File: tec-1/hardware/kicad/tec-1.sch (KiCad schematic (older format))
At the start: 34 parts

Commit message: tec-1/hardware/kicad: progress checkin
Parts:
- removed C? (x4): 0.1uF/10V, symbol tec-1:C
- removed C?: 100uF/10V, symbol tec-1:C
- removed FB?: Ferrite_Bead_Small, symbol tec-1:Ferrite_Bead_Small
- removed J?: USB_C_Receptacle_USB2.0, symbol tec-1:USB_C_Receptacle_USB2.0
- removed R?: 100k, symbol tec-1:R
- removed R? (x2): 5.1k, symbol tec-1:R
- removed U?: ADDRESS, symbol tec-1:ADDRESS
- removed U?: KEYDB, symbol tec-1:KEYDB
- removed U?: FT232RL, Package_SO:SSOP-28_5.3x10.2mm_P0.65mm, symbol tec-1:FT232RL
- added C1: 0.1uF/10V, tec-1:C_0805_2012Metric, symbol tec-1:C
- added TP1, TP10, TP11, TP12, TP13, TP14, TP15, TP16, TP17, TP18, TP19, TP2, TP20, TP3, TP4, TP5, TP6, TP7, TP8, TP9: TestPoint, tec-1:TestPoint_Pad_D2.0mm, symbol tec-1:TestPoint
- added U1: IO, tec-1:PLCC-28_SMD-Socket, symbol tec-1:IO
- added U2: MEMORY, tec-1:PLCC-28_SMD-Socket, symbol tec-1:MEMORY
- C2, C3, C4, C5, C6: renamed from C?; footprint (none) -> tec-1:C_0805_2012Metric
- R1, R10, R11, R2, R3, R4, R5, R6, R7, R8, R9: renamed from R?; footprint (none) -> tec-1:R_0805_2012Metric
- SW1: renamed from SW?; footprint (none) -> tec-1:DIP-8_W7.62mm_LongPads
- U3: renamed from U?; footprint (none) -> tec-1:DIP-40_W15.24mm_LongPads
- U5, U6: renamed from U?; footprint Package_DIP:DIP-28_W15.24mm -> tec-1:DIP-28_W15.24mm_LongPads
- gave numbers to parts that had none: 1
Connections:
- net labels added: LCD_E, ~MATRIXCOL_G_CS, ~MATRIXCOL_R_CS, ~MATRIXROW_CS, ~SEG7COL_CS, ~SEG7ROW_CS
- net labels removed: FTDI_D0, FTDI_D1, FTDI_D2, FTDI_D3, FTDI_D5, FTDI_D6, FTDI_D7, VBUS
- wire segments 103 -> 123
- no-connect marks 19 -> 14
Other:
- moved on the sheet: C2, R5, R6, R7, R8, SW1

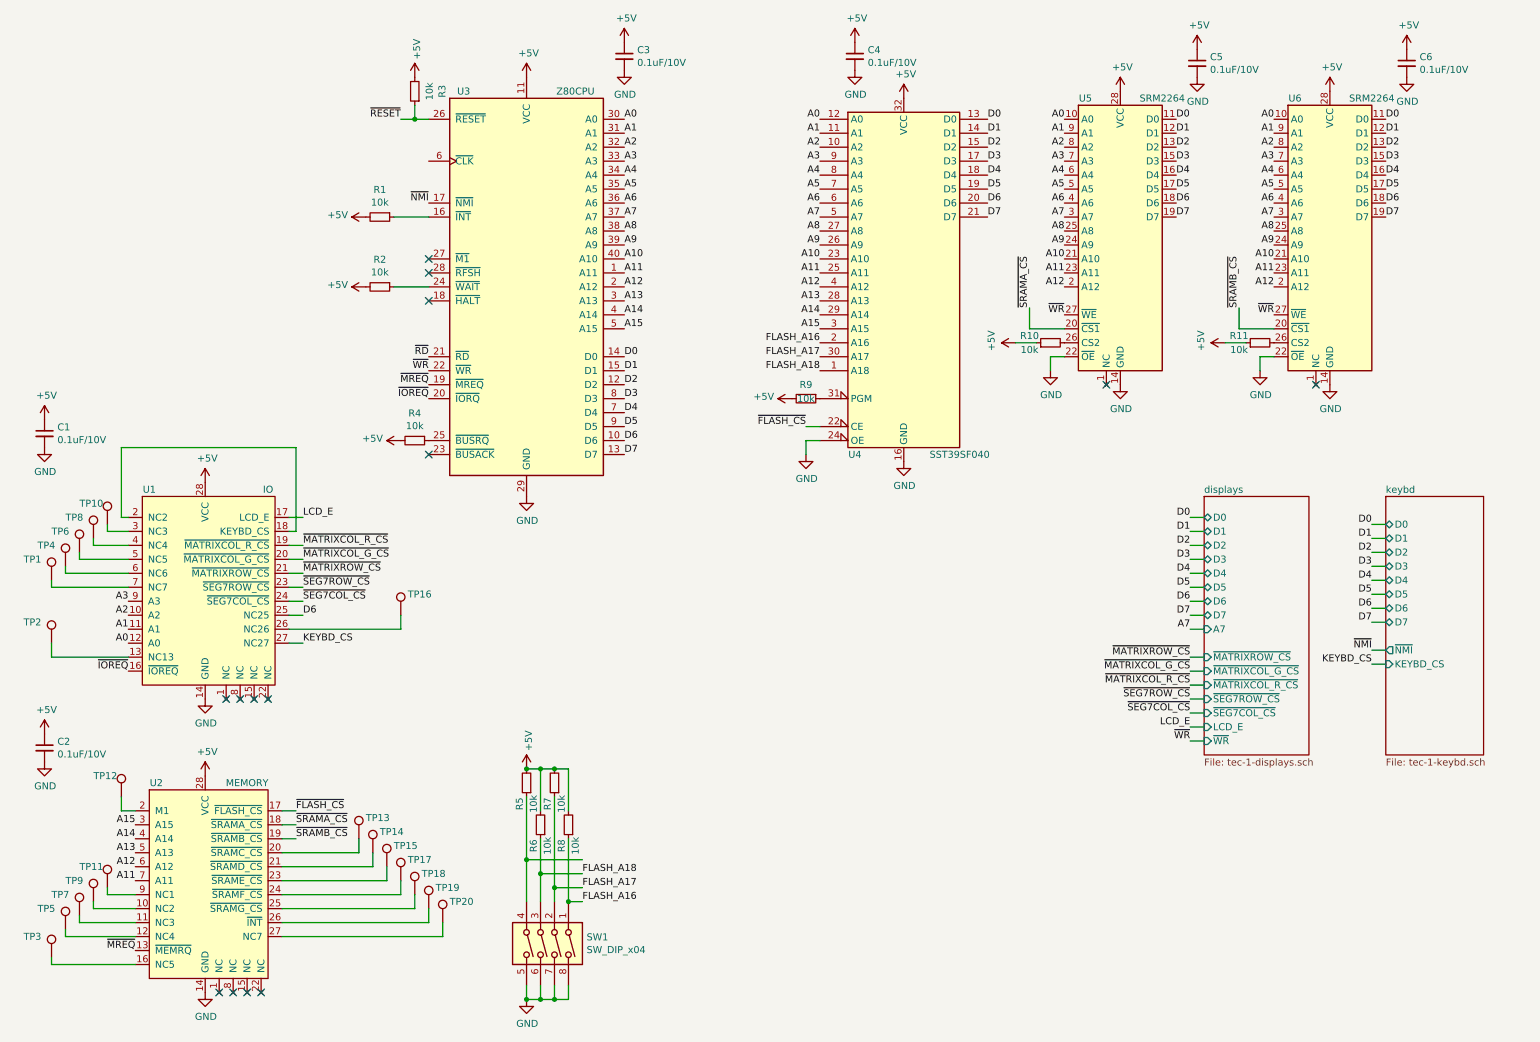
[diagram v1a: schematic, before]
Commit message: tec-1/hardware/kicad: progress checkin - add clock & 207 unrouted
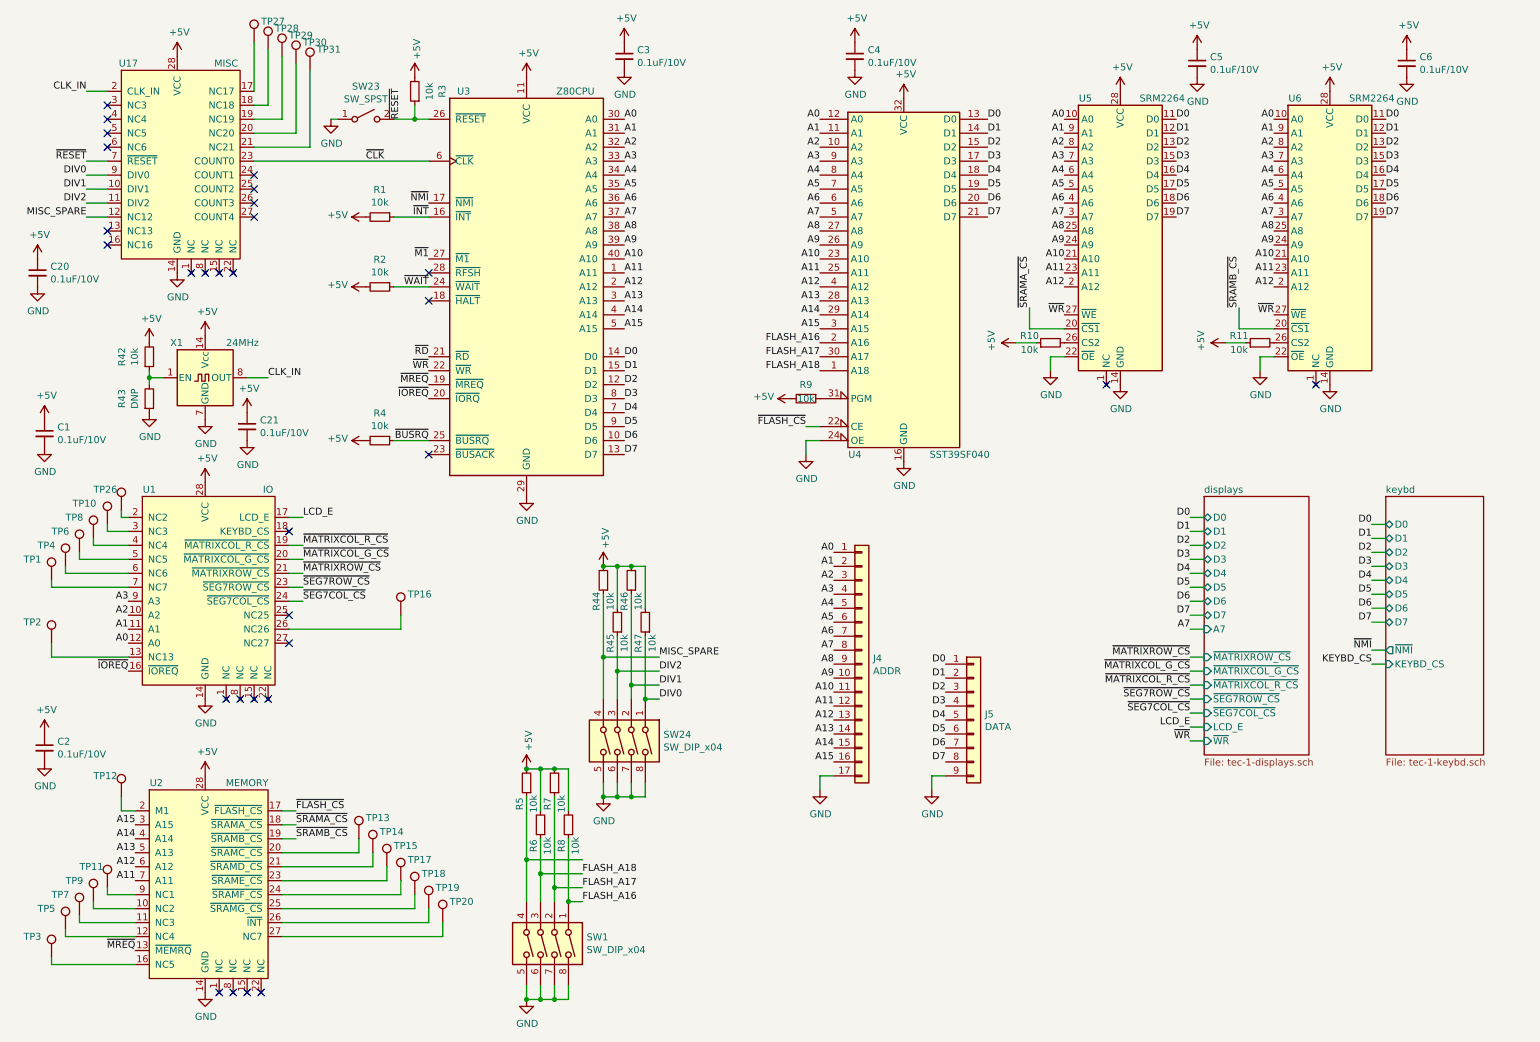
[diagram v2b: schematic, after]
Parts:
- added C20, C21: 0.1uF/10V, tec-1:C_0805_2012Metric, symbol tec-1:C
- added J4: ADDR, tec-1:PinHeader_1x17_P2.54mm_Vertical, symbol tec-1:Conn_01x17
- added J5: DATA, tec-1:PinHeader_1x09_P2.54mm_Vertical, symbol tec-1:Conn_01x09
- added R42, R44, R45, R46, R47: 10k, tec-1:R_0805_2012Metric, symbol tec-1:R
- added R43: DNP, tec-1:R_0805_2012Metric, symbol tec-1:R
- added SW23: SW_SPST, tec-1:SW_12x12_SMD, symbol tec-1:SW_SPST
- added SW24: SW_DIP_x04, tec-1:DIP-8_W7.62mm_LongPads, symbol tec-1:SW_DIP_x04
- added TP26, TP27, TP28, TP29, TP30, TP31: TestPoint, tec-1:TestPoint_Pad_D2.0mm, symbol tec-1:TestPoint
- added U17: MISC, tec-1:PLCC-28_SMD-Socket, symbol tec-1:MISC
- added X1: 24MHz, tec-1:Oscillator_DIP-14_LargePads, symbol tec-1:CXO_DIP14
- U4: footprint (none) -> tec-1:PLCC-32_SMD-Socket_9x7
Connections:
- net +5V: now also C20.1, C21.1, R42.2, R44.2, R45.2, R46.2, R47.2, U17.28 (VCC), X1.14 (Vcc)
- net A0: now also J4.1 (Pin_1)
- net A1: now also J4.2 (Pin_2)
- net A10: now also J4.11 (Pin_11)
- net A11: now also J4.12 (Pin_12)
- net A12: now also J4.13 (Pin_13)
- net A13: now also J4.14 (Pin_14)
- net A14: now also J4.15 (Pin_15)
- net A15: now also J4.16 (Pin_16)
- net A2: now also J4.3 (Pin_3)
- net A3: now also J4.4 (Pin_4)
- net A4: now also J4.5 (Pin_5)
- net A5: now also J4.6 (Pin_6)
- net A6: now also J4.7 (Pin_7)
- net A7: now also J4.8 (Pin_8)
- net A8: now also J4.9 (Pin_9)
- net A9: now also J4.10 (Pin_10)
- net D0: now also J5.1 (Pin_1)
- net D1: now also J5.2 (Pin_2)
- net D2: now also J5.3 (Pin_3)
- net D3: now also J5.4 (Pin_4)
- net D4: now also J5.5 (Pin_5)
- net D5: now also J5.6 (Pin_6)
- net D6: now also J5.7 (Pin_7); no longer U1.25 (NC25)
- net D7: now also J5.8 (Pin_8)
- net GND: now also C20.2, C21.2, J4.17 (Pin_17), J5.9 (Pin_9), R43.1, SW23.1 (A), SW24.5, SW24.6, SW24.7, SW24.8, U17.14 (GND), X1.7 (GND)
- net KEYBD_CS: no longer U1.27 (NC27)
- net ~RESET: now also SW23.2 (B), U17.7 (~RESET)
- net ~INT: now reaches R1.1, U3.16 (~INT~)
- net ~WAIT: now reaches R2.1, U3.24 (~WAIT~)
- net ~BUSRQ: now reaches R4.1, U3.25 (~BUSRQ~)
- net ~M1: now reaches U3.27 (~M1~)
- net ~CLK: now reaches U3.6 (~CLK~)
- net ~CLK: now also U17.23 (COUNT0)
- net at U1.18 (KEYBD_CS): no longer U1.2 (NC2)
- new net: TP27.1, U17.17 (NC17)
- new net: TP28.1, U17.18 (NC18)
- new net: TP29.1, U17.19 (NC19)
- new net: TP30.1, U17.20 (NC20)
- new net: TP31.1, U17.21 (NC21)
- new net: R42.1, R43.2, X1.1 (EN)
- new net: TP26.1, U1.2 (NC2)
- new net CLK_IN: U17.2 (CLK_IN), X1.8 (OUT)
- new net DIV0: R47.1, SW24.1, U17.9 (DIV0)
- new net DIV1: R46.1, SW24.2, U17.10 (DIV1)
- new net DIV2: R45.1, SW24.3, U17.11 (DIV2)
- new net MISC_SPARE: R44.1, SW24.4, U17.12 (NC12)
- no-connect marks 14 -> 30
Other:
- moved on the sheet: R4

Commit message: tec-1/hardware/kicad: routing complete, all DRC errors checked as ok
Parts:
- removed TP10, TP11, TP12, TP14, TP15, TP17, TP19, TP20, TP26, TP4, TP6, TP7, TP8, TP9: TestPoint, tec-1:TestPoint_Pad_D2.0mm, symbol tec-1:TestPoint
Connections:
- net KEYBD_CS: now also U1.18 (KEYBD_CS)
- net ~INT: now also U2.26 (~INT)
- net ~M1: now also U2.2 (M1)
- no-connect marks 30 -> 42
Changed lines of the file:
@@
 Text Label 4800 3650 0    50   ~ 0
 D7
-Text Label 3400 2950 2    50   ~ 0
-~RD
 Text Label 3400 3050 2    50   ~ 0
 ~WR
@@
 	1    0    0    -1
 $EndComp
-$Comp
-L tec-1:TestPoint TP7
-U 1 1 60BE6F95
-P 900 6950
-F 0 "TP7" H 700 7100 50  0000 L CNN
-F 1 "TestPoint" H 958 6977 50  0001 L CNN
-F 2 "tec-1:TestPoint_Pad_D2.0mm" H 1100 6950 50  0001 C CNN
-F 3 "~" H 1100 6950 50  0001 C CNN
-	1    900  6950
-	1    0    0    -1
-$EndComp
-$Comp
-L tec-1:TestPoint TP9
-U 1 1 60BEA0AC
-P 1000 6850
-F 0 "TP9" H 800 7000 50  0000 L CNN
-F 1 "TestPoint" H 1058 6877 50  0001 L CNN
-F 2 "tec-1:TestPoint_Pad_D2.0mm" H 1200 6850 50  0001 C CNN
-F 3 "~" H 1200 6850 50  0001 C CNN
-	1    1000 6850
-	1    0    0    -1
-$EndComp
-$Comp
-L tec-1:TestPoint TP11
-U 1 1 60BEA26C
-P 1100 6750
-F 0 "TP11" H 900 6900 50  0000 L CNN
-F 1 "TestPoint" H 1158 6777 50  0001 L CNN
-F 2 "tec-1:TestPoint_Pad_D2.0mm" H 1300 6750 50  0001 C CNN
-F 3 "~" H 1300 6750 50  0001 C CNN
-	1    1100 6750
-	1    0    0    -1
-$EndComp
-Wire Wire Line
-	1300 6800 1100 6800
-Wire Wire Line
-	1100 6800 1100 6750
-Wire Wire Line
-	1000 6850 1000 6900
-Wire Wire Line
-	1000 6900 1300 6900
-Wire Wire Line
-	1300 7000 900  7000
-Wire Wire Line
-	900  7000 900  6950
 Wire Wire Line
 	1300 7100 800  7100
@@
 	700  7300 1300 7300
 $Comp
-L tec-1:TestPoint TP12
-U 1 1 60BF99B1
-P 1200 6100
-F 0 "TP12" H 1000 6250 50  0000 L CNN
-F 1 "TestPoint" H 1258 6127 50  0001 L CNN
-F 2 "tec-1:TestPoint_Pad_D2.0mm" H 1400 6100 50  0001 C CNN
-F 3 "~" H 1400 6100 50  0001 C CNN
-	1    1200 6100
-	1    0    0    -1
-$EndComp
-Wire Wire Line
-	1200 6100 1200 6200
-Wire Wire Line
-	1200 6200 1300 6200
-$Comp
 L tec-1:TestPoint TP13
 U 1 1 60C03715
@@
 $EndComp
 $Comp
-L tec-1:TestPoint TP14
-U 1 1 60C068C6
-P 3000 6500
-F 0 "TP14" H 3050 6650 50  0000 L CNN
-F 1 "TestPoint" H 3058 6527 50  0001 L CNN
-F 2 "tec-1:TestPoint_Pad_D2.0mm" H 3200 6500 50  0001 C CNN
-F 3 "~" H 3200 6500 50  0001 C CNN
-	1    3000 6500
-	1    0    0    -1
-$EndComp
-$Comp
-L tec-1:TestPoint TP15
-U 1 1 60C06CE2
-P 3100 6600
-F 0 "TP15" H 3150 6750 50  0000 L CNN
-F 1 "TestPoint" H 3158 6627 50  0001 L CNN
-F 2 "tec-1:TestPoint_Pad_D2.0mm" H 3300 6600 50  0001 C CNN
-F 3 "~" H 3300 6600 50  0001 C CNN
-	1    3100 6600
-	1    0    0    -1
-$EndComp
-$Comp
-L tec-1:TestPoint TP17
-U 1 1 60C07071
-P 3200 6700
-F 0 "TP17" H 3250 6850 50  0000 L CNN
-F 1 "TestPoint" H 3258 6727 50  0001 L CNN
-F 2 "tec-1:TestPoint_Pad_D2.0mm" H 3400 6700 50  0001 C CNN
-F 3 "~" H 3400 6700 50  0001 C CNN
-	1    3200 6700
-	1    0    0    -1
-$EndComp
-$Comp
 L tec-1:TestPoint TP18
 U 1 1 60C074D6
@@
 	1    0    0    -1
 $EndComp
-$Comp
-L tec-1:TestPoint TP19
-U 1 1 60C07975
-P 3400 6900
-F 0 "TP19" H 3450 7050 50  0000 L CNN
-F 1 "TestPoint" H 3458 6927 50  0001 L CNN
-F 2 "tec-1:TestPoint_Pad_D2.0mm" H 3600 6900 50  0001 C CNN
-F 3 "~" H 3600 6900 50  0001 C CNN
-	1    3400 6900
-	1    0    0    -1
-$EndComp
-$Comp
-L tec-1:TestPoint TP20
-U 1 1 60C07D6A
-P 3500 7000
-F 0 "TP20" H 3550 7150 50  0000 L CNN
-F 1 "TestPoint" H 3558 7027 50  0001 L CNN
-F 2 "tec-1:TestPoint_Pad_D2.0mm" H 3700 7000 50  0001 C CNN
-F 3 "~" H 3700 7000 50  0001 C CNN
-	1    3500 7000
-	1    0    0    -1
-$EndComp
 Wire Wire Line
 	2350 6500 2900 6500
@@
 	2900 6500 2900 6400
 Wire Wire Line
-	2350 6600 3000 6600
-Wire Wire Line
-	3000 6600 3000 6500
-Wire Wire Line
-	2350 6700 3100 6700
-Wire Wire Line
-	3100 6700 3100 6600
-Wire Wire Line
-	2350 6800 3200 6800
-Wire Wire Line
-	3200 6800 3200 6700
-Wire Wire Line
 	2350 6900 3300 6900
 Wire Wire Line
 	3300 6900 3300 6800
-Wire Wire Line
-	2350 7000 3400 7000
-Wire Wire Line
-	3400 7000 3400 6900
-Wire Wire Line
-	2350 7100 3500 7100
-Wire Wire Line
-	3500 7100 3500 7000
 $Comp
 L tec-1:IO U1
@@
 	1    0    0    -1
 $EndComp
-$Comp
-L tec-1:TestPoint TP4
-U 1 1 60D0AC7B
-P 800 4450
-F 0 "TP4" H 600 4600 50  0000 L CNN
-F 1 "TestPoint" H 858 4477 50  0001 L CNN
-F 2 "tec-1:TestPoint_Pad_D2.0mm" H 1000 4450 50  0001 C CNN
-F 3 "~" H 1000 4450 50  0001 C CNN
-	1    800  4450
-	1    0    0    -1
-$EndComp
-$Comp
-L tec-1:TestPoint TP6
-U 1 1 60D0AC85
-P 900 4350
-F 0 "TP6" H 700 4500 50  0000 L CNN
-F 1 "TestPoint" H 958 4377 50  0001 L CNN
-F 2 "tec-1:TestPoint_Pad_D2.0mm" H 1100 4350 50  0001 C CNN
-F 3 "~" H 1100 4350 50  0001 C CNN
-	1    900  4350
-	1    0    0    -1
-$EndComp
-$Comp
-L tec-1:TestPoint TP8
-U 1 1 60D0AC8F
-P 1000 4250
-F 0 "TP8" H 800 4400 50  0000 L CNN
-F 1 "TestPoint" H 1058 4277 50  0001 L CNN
-F 2 "tec-1:TestPoint_Pad_D2.0mm" H 1200 4250 50  0001 C CNN
-F 3 "~" H 1200 4250 50  0001 C CNN
-	1    1000 4250
-	1    0    0    -1
-$EndComp
-Wire Wire Line
-	1250 4300 1000 4300
-Wire Wire Line
-	1000 4300 1000 4250
-Wire Wire Line
-	900  4350 900  4400
-Wire Wire Line
-	900  4400 1250 4400
-Wire Wire Line
-	1250 4500 800  4500
-Wire Wire Line
-	800  4500 800  4450
 Wire Wire Line
 	1250 4600 700  4600
@@
 Wire Wire Line
 	700  5000 700  5100
-$Comp
-L tec-1:TestPoint TP10
-U 1 1 60D327B7
-P 1100 4150
-F 0 "TP10" H 850 4300 50  0000 L CNN
-F 1 "TestPoint" H 1158 4177 50  0001 L CNN
-F 2 "tec-1:TestPoint_Pad_D2.0mm" H 1300 4150 50  0001 C CNN
-F 3 "~" H 1300 4150 50  0001 C CNN
-	1    1100 4150
-	1    0    0    -1
-$EndComp
-Wire Wire Line
-	1250 4200 1100 4200
-Wire Wire Line
-	1100 4200 1100 4150
 Text Label 1250 5000 2    50   ~ 0
 A0
@@
 Wire Wire Line
 	6200 5950 6200 6050
-$Comp
-L tec-1:TestPoint TP26
-U 1 1 62206534
-P 1200 4050
-F 0 "TP26" H 1000 4200 50  0000 L CNN
-F 1 "TestPoint" H 1258 4077 50  0001 L CNN
-F 2 "tec-1:TestPoint_Pad_D2.0mm" H 1400 4050 50  0001 C CNN
-F 3 "~" H 1400 4050 50  0001 C CNN
-	1    1200 4050
-	1    0    0    -1
-$EndComp
-Wire Wire Line
-	1200 4050 1200 4100
-Wire Wire Line
-	1200 4100 1250 4100
 NoConn ~ 2400 5000
 NoConn ~ 2400 4800
-NoConn ~ 2400 4200
 Text Label 10150 5050 2    50   ~ 0
 ~NMI
@@
 	1    0    0    -1
 $EndComp
+NoConn ~ 1250 4100
+NoConn ~ 1250 4200
+NoConn ~ 1250 4300
+NoConn ~ 1250 4400
+NoConn ~ 1250 4500
+NoConn ~ 1300 6900
+NoConn ~ 1300 7000
+NoConn ~ 1300 6800
+NoConn ~ 2350 6600
+NoConn ~ 2350 6700
+NoConn ~ 2350 6800
+NoConn ~ 2350 7100
+Text Label 3400 2950 2    50   ~ 0
+~RD
+NoConn ~ 3400 2950
+Wire Wire Line
+	2400 4200 2500 4200
+Text Label 2500 4200 0    50   ~ 0
+KEYBD_CS
+Text Label 1300 6200 2    50   ~ 0
+~M1
+Wire Wire Line
+	2350 7000 2450 7000
+Text Label 2450 7000 0    50   ~ 0
+~INT
 $EndSCHEMATC

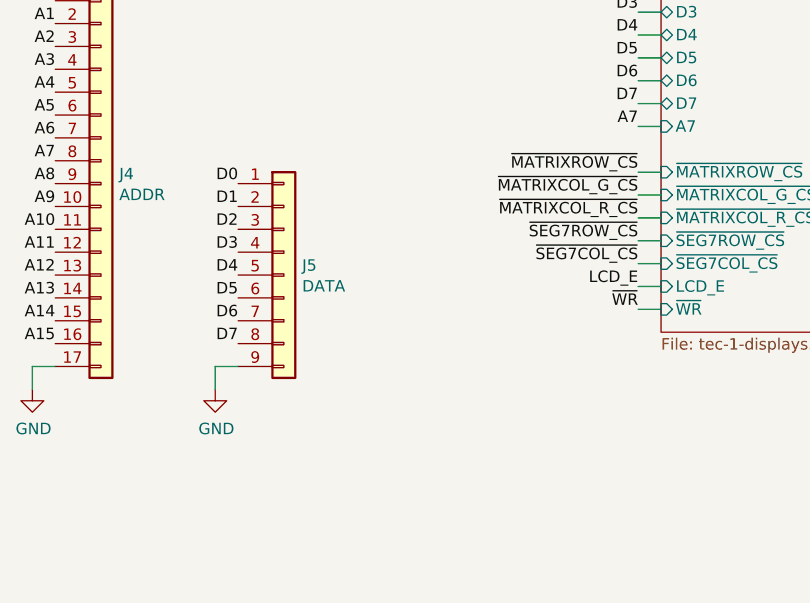
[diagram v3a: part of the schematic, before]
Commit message: tec-1/hardware/kicad: added ctrl header, fixed keypad alignment
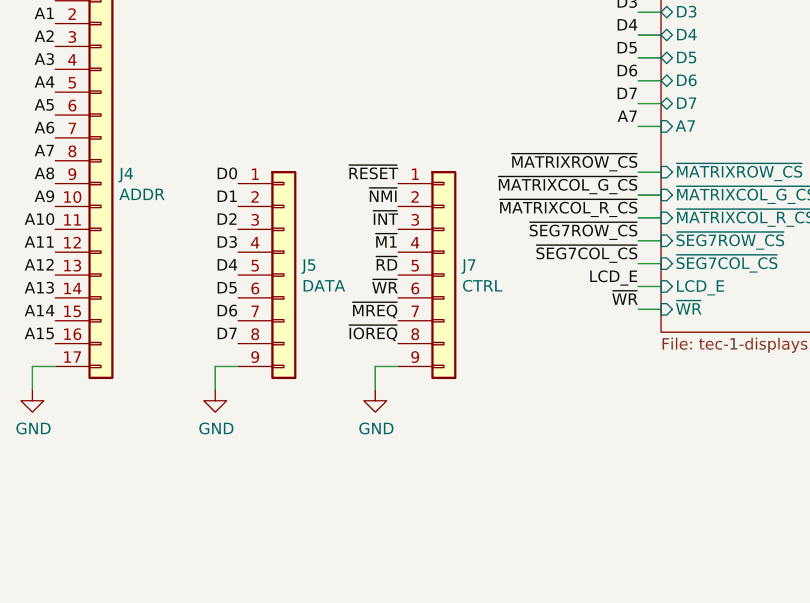
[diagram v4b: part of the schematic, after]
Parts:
- added J7: CTRL, tec-1:PinHeader_1x09_P2.54mm_Vertical, symbol tec-1:Conn_01x09
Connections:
- net GND: now also J7.9 (Pin_9)
- net ~INT: now also J7.3 (Pin_3)
- net ~IOREQ: now also J7.8 (Pin_8)
- net ~M1: now also J7.4 (Pin_4)
- net ~MREQ: now also J7.7 (Pin_7)
- net ~NMI: now also J7.2 (Pin_2)
- net ~RD: now also J7.5 (Pin_5)
- net ~RESET: now also J7.1 (Pin_1)
- net ~WR: now also J7.6 (Pin_6)
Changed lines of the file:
@@
 Text Label 2450 7000 0    50   ~ 0
 ~INT
+$Comp
+L tec-1:Conn_01x09 J7
+U 1 1 608ADCE2
+P 8000 5550
+F 0 "J7" H 8080 5592 50  0000 L CNN
+F 1 "CTRL" H 8080 5501 50  0000 L CNN
+F 2 "tec-1:PinHeader_1x09_P2.54mm_Vertical" H 8000 5550 50  0001 C CNN
+F 3 "~" H 8000 5550 50  0001 C CNN
+	1    8000 5550
+	1    0    0    -1
+$EndComp
+$Comp
+L power:GND #PWR0136
+U 1 1 608B02EE
+P 7700 6050
+F 0 "#PWR0136" H 7700 5800 50  0001 C CNN
+F 1 "GND" H 7705 5877 50  0000 C CNN
+F 2 "" H 7700 6050 50  0001 C CNN
+F 3 "" H 7700 6050 50  0001 C CNN
+	1    7700 6050
+	1    0    0    -1
+$EndComp
+Wire Wire Line
+	7800 5950 7700 5950
+Wire Wire Line
+	7700 5950 7700 6050
+Text Label 7800 5650 2    50   ~ 0
+~WR
+Text Label 7800 5750 2    50   ~ 0
+~MREQ
+Text Label 7800 5850 2    50   ~ 0
+~IOREQ
+Text Label 7800 5550 2    50   ~ 0
+~RD
+Text Label 7800 5450 2    50   ~ 0
+~M1
+Text Label 7800 5250 2    50   ~ 0
+~NMI
+Text Label 7800 5350 2    50   ~ 0
+~INT
+Text Label 7800 5150 2    50   ~ 0
+~RESET
 $EndSCHEMATC

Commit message: tec-1/hardware/kicad: regenerate Apr2021 release with missing edge cuts included
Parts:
- X1: LCSC (none) -> DNP
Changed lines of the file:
@@
 Sheet 1 3
 Title ""
-Date ""
-Rev ""
+Date "2021-04-15"
+Rev "Apr2021"
 Comp ""
 Comment1 ""
@@
 F 2 "tec-1:Oscillator_DIP-14_LargePads" H 2250 2750 50  0001 C CNN
 F 3 "http://cdn-reichelt.de/documents/datenblatt/B400/OSZI.pdf" H 1700 3100 50  0001 C CNN
+F 4 "DNP" H 1800 3100 50  0001 C CNN "LCSC"
 	1    1800 3100
 	1    0    0    -1
